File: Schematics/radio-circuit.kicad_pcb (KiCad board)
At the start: 4 copper layers, 54 x 26.5 mm, 44 parts, among them J1 USB_A, J2 STDC14, J3 0, U1 USBLC6-2SC6, U2 LD39015M33R, U3 STM32F042F6Px, U4 Si4705-D60-GM, Y1 SG-3030CM

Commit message: Added JLCPCB mounting holes
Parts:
- added H1: MountingHole, Local:MountingHole_JLCPCB, F.Cu at (164.2, 114.2)
- added H2: MountingHole, Local:MountingHole_JLCPCB, F.Cu at (213.8, 114.2)
- added H3: MountingHole, Local:MountingHole_JLCPCB, F.Cu at (213.8, 136.2)
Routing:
- net GND: track 46.3 -> 43.8 mm, vias 95 -> 90

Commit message: Replaced USB-connector with a different one
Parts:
- J1: footprint Local:USB_A_Molex_48037-2200_Horizontal -> Local:USB_A_AM180-01-T1-W
- moved C5 0.25 mm to (170.9, 119.1)
- moved J2 0.24 mm to (177.8, 115.6)
- moved J3 0.22 mm to (211.5, 125.2)
- moved R10 0.20 mm to (198.3, 118.4)
- moved R12 0.20 mm to (188.9, 117.4)
- moved R2 0.20 mm to (195.9, 118.4)
- moved R5 0.20 mm to (183.8, 134.1)
- moved C1 0.20 mm to (164.2, 134.2)
- moved C10 0.20 mm to (193.5, 118.4)
- moved C11 0.20 mm to (188.4, 122.0)
- moved C12 0.20 mm to (188.9, 123.5)
- moved C13 0.20 mm to (192.9, 128.0)
- moved C14 0.20 mm to (194.9, 125.8)
- moved C15 0.20 mm to (191.2, 127.5)
- moved C16 0.20 mm to (201.2, 125.2)
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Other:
- board size 54 x 26.5 mm -> 54.2 x 26.5 mm

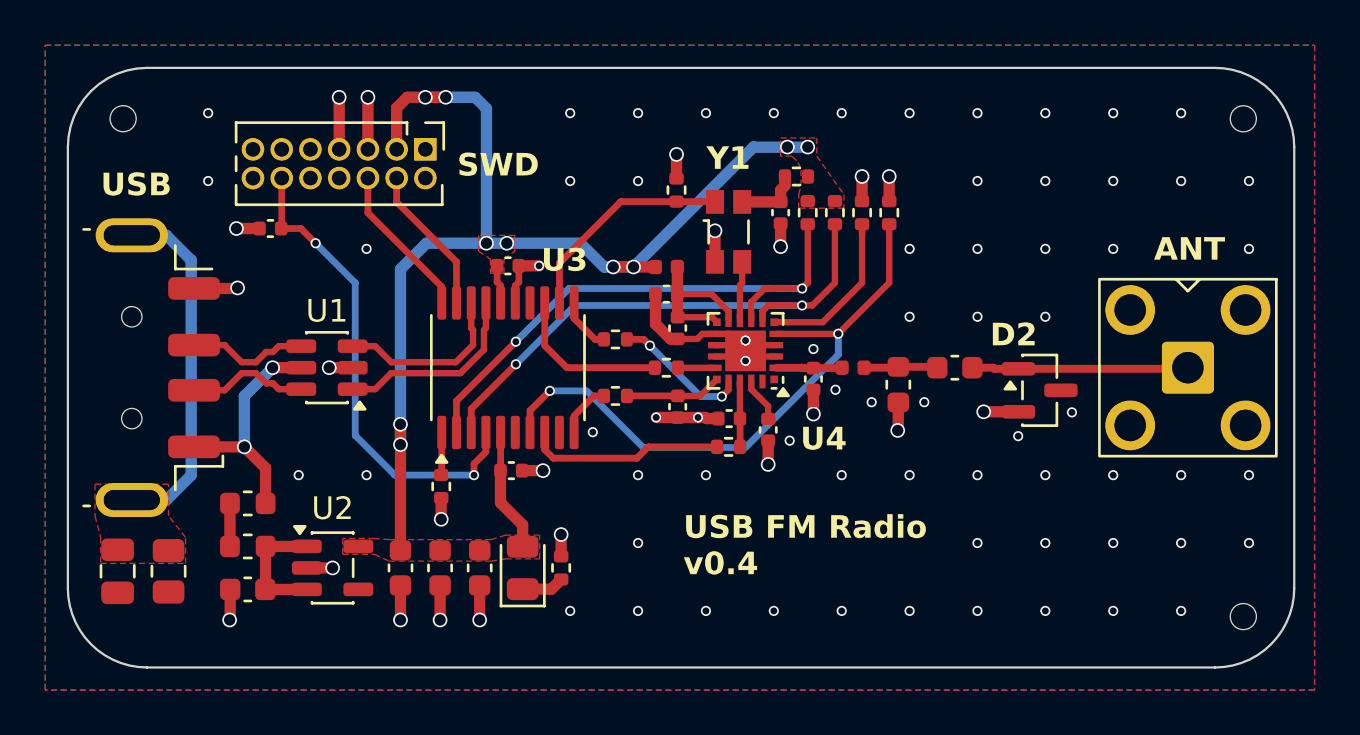
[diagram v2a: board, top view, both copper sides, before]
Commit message: Adjusted via locations and USB-connector footprint
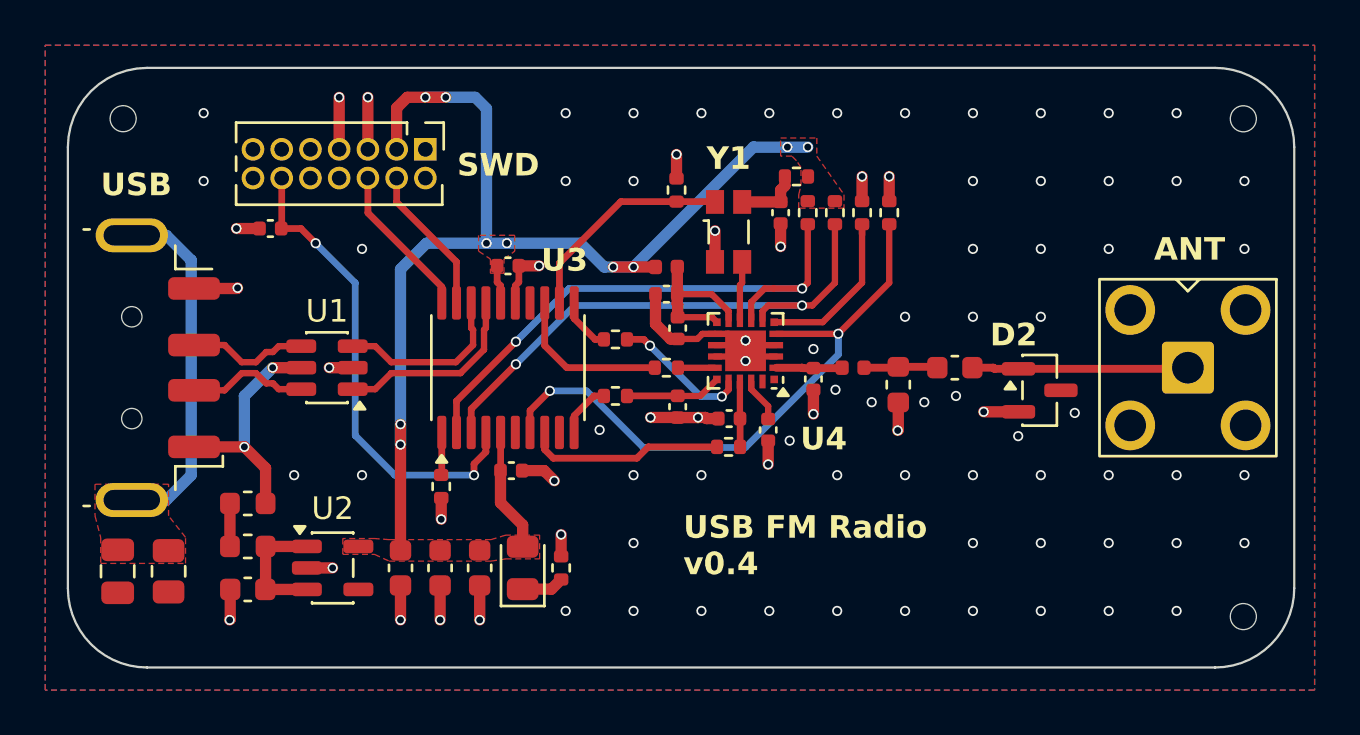
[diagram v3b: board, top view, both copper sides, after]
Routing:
- net GND: track 43.8 -> 44.8 mm

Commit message: Cleared tracks overlapping pads
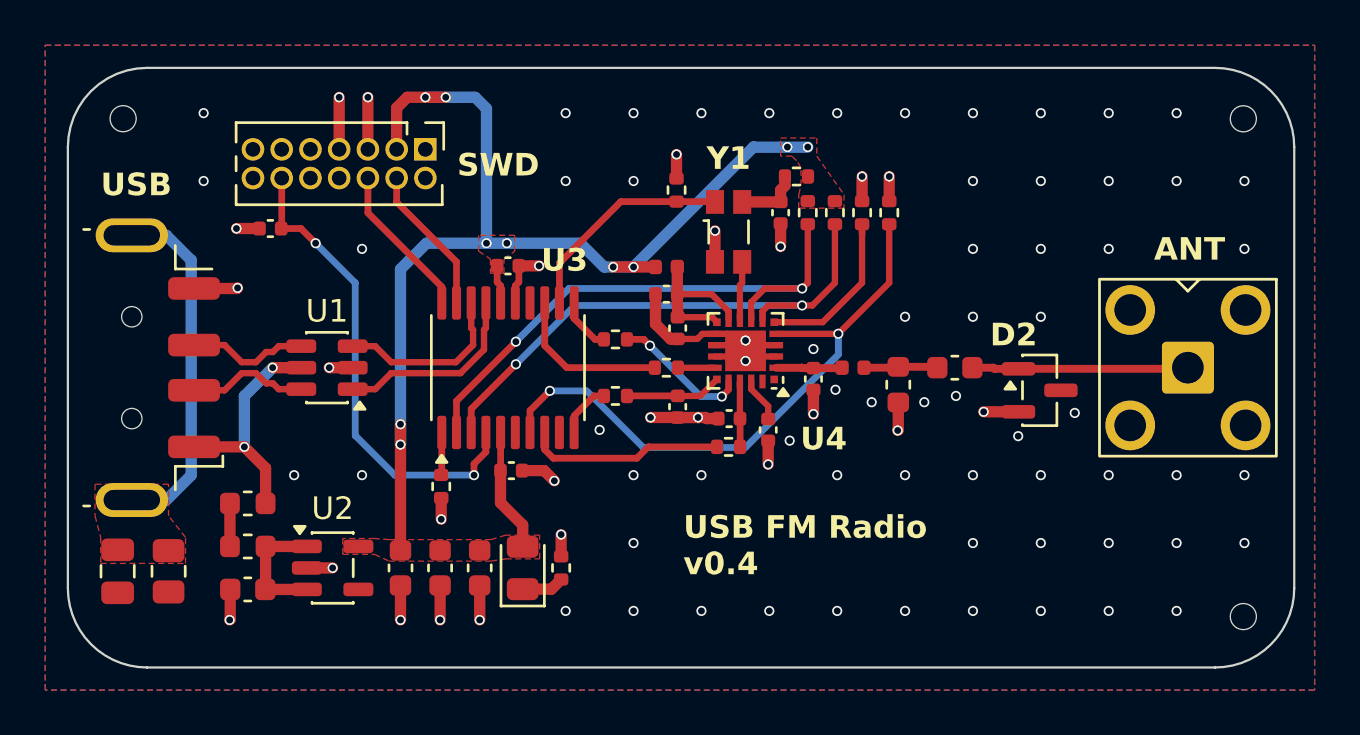
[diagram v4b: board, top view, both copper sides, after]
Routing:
- net GND: track 44.8 -> 43.2 mm
